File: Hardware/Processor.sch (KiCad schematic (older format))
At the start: 15 parts, among them J1 ICSP-PIC, J2 USB_MINI, SW1 PGM, SW2 RST, U5 PIC32MX250F128B, X1 8MHz

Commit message: Initial component mapping
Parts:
- J2: Distributor Part No (none) -> ED2992CT-ND; MFR Name (none) -> On Shore Technology; MFR Part No (none) -> USB-M26FTR
- X1: Distributor Part No (none) -> 535-9831-1-ND; MFR Name (none) -> Abracon; MFR Part No (none) -> ABM7-8.000MHZ-D2Y-T
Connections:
- wire segments 72 -> 63
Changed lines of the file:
@@
 $EndComp
 $Comp
-L +3.3V #PWR32
+L +3.3V #PWR031
 U 1 1 5240FDA6
 P 2500 1800
-F 0 "#PWR32" H 2500 1760 30  0001 C CNN
+F 0 "#PWR031" H 2500 1760 30  0001 C CNN
 F 1 "+3.3V" H 2500 1910 30  0000 C CNN
 F 2 "" H 2500 1800 60  0000 C CNN
@@
 $EndComp
 $Comp
-L GND #PWR35
+L GND #PWR032
 U 1 1 5240FDF5
 P 2500 3100
-F 0 "#PWR35" H 2500 3100 30  0001 C CNN
+F 0 "#PWR032" H 2500 3100 30  0001 C CNN
 F 1 "GND" H 2500 3030 30  0001 C CNN
 F 2 "" H 2500 3100 60  0000 C CNN
@@
 F 2 "~" H 2450 5200 60  0000 C CNN
 F 3 "~" H 2450 5200 60  0000 C CNN
+F 4 "Abracon" H 2450 5200 60  0001 C CNN "MFR Name"
+F 5 "ABM7-8.000MHZ-D2Y-T" H 2450 5200 60  0001 C CNN "MFR Part No"
+F 6 "535-9831-1-ND" H 2450 5200 60  0001 C CNN "Distributor Part No"
 	1    2450 5200
 	1    0    0    -1
@@
 OSC2
 $Comp
-L GND #PWR41
+L GND #PWR033
 U 1 1 5240FF54
 P 2100 5900
-F 0 "#PWR41" H 2100 5900 30  0001 C CNN
+F 0 "#PWR033" H 2100 5900 30  0001 C CNN
 F 1 "GND" H 2100 5830 30  0001 C CNN
 F 2 "" H 2100 5900 60  0000 C CNN
@@
 $EndComp
 $Comp
-L GND #PWR42
+L GND #PWR034
 U 1 1 5240FF63
 P 2800 5900
-F 0 "#PWR42" H 2800 5900 30  0001 C CNN
+F 0 "#PWR034" H 2800 5900 30  0001 C CNN
 F 1 "GND" H 2800 5830 30  0001 C CNN
 F 2 "" H 2800 5900 60  0000 C CNN
@@
 F 2 "~" H 2000 3850 60  0000 C CNN
 F 3 "~" H 2000 3850 60  0000 C CNN
+F 4 "On Shore Technology" H 2000 3850 60  0001 C CNN "MFR Name"
+F 5 "USB-M26FTR" H 2000 3850 60  0001 C CNN "MFR Part No"
+F 6 "ED2992CT-ND" H 2000 3850 60  0001 C CNN "Distributor Part No"
 	1    2000 3850
 	-1   0    0    -1
@@
 $EndComp
 $Comp
-L +3.3V #PWR37
+L +3.3V #PWR035
 U 1 1 5240FFFE
 P 6800 3300
-F 0 "#PWR37" H 6800 3260 30  0001 C CNN
+F 0 "#PWR035" H 6800 3260 30  0001 C CNN
 F 1 "+3.3V" H 6800 3410 30  0000 C CNN
 F 2 "" H 6800 3300 60  0000 C CNN
@@
 $EndComp
 $Comp
-L GND #PWR40
+L GND #PWR036
 U 1 1 52410043
 P 6900 4900
-F 0 "#PWR40" H 6900 4900 30  0001 C CNN
+F 0 "#PWR036" H 6900 4900 30  0001 C CNN
 F 1 "GND" H 6900 4830 30  0001 C CNN
 F 2 "" H 6900 4900 60  0000 C CNN
@@
 $EndComp
 $Comp
-L +3.3V #PWR36
+L +3.3V #PWR037
 U 1 1 524100A6
 P 5400 3300
-F 0 "#PWR36" H 5400 3260 30  0001 C CNN
+F 0 "#PWR037" H 5400 3260 30  0001 C CNN
 F 1 "+3.3V" H 5400 3410 30  0000 C CNN
 F 2 "" H 5400 3300 60  0000 C CNN
@@
 $EndComp
 $Comp
-L GND #PWR39
+L GND #PWR038
 U 1 1 524100D5
 P 5300 4900
-F 0 "#PWR39" H 5300 4900 30  0001 C CNN
+F 0 "#PWR038" H 5300 4900 30  0001 C CNN
 F 1 "GND" H 5300 4830 30  0001 C CNN
 F 2 "" H 5300 4900 60  0000 C CNN
@@
 $EndComp
 $Comp
-L GND #PWR44
+L GND #PWR039
 U 1 1 5241010B
 P 2100 7200
-F 0 "#PWR44" H 2100 7200 30  0001 C CNN
+F 0 "#PWR039" H 2100 7200 30  0001 C CNN
 F 1 "GND" H 2100 7130 30  0001 C CNN
 F 2 "" H 2100 7200 60  0000 C CNN
@@
 $EndComp
 Wire Wire Line
-	2500 1800 2500 1900
-Wire Wire Line
-	2500 1900 2500 2700
+	2500 1800 2500 2700
 Wire Wire Line
 	2500 2700 2400 2700
@@
 	2500 2800 2500 3100
 Wire Wire Line
-	2400 2600 2700 2600
-Wire Wire Line
-	2700 2600 2800 2600
+	2400 2600 2800 2600
 Wire Wire Line
 	2700 2500 2700 2600
@@
 	2400 3000 2800 3000
 Wire Wire Line
-	2800 5100 2800 5200
-Wire Wire Line
-	2800 5200 2800 5300
-Wire Wire Line
-	2100 5100 2100 5200
-Wire Wire Line
-	2100 5200 2100 5300
+	2800 5100 2800 5300
+Wire Wire Line
+	2100 5100 2100 5300
 Wire Wire Line
 	2200 5200 2100 5200
@@
 	7000 3600 6700 3600
 Wire Wire Line
-	6800 3300 6800 3700
-Wire Wire Line
-	6800 3700 6800 4300
+	6800 3300 6800 4300
 Wire Wire Line
 	6800 3700 6700 3700
 Wire Wire Line
-	6900 3800 6900 4700
-Wire Wire Line
-	6900 4700 6900 4900
+	6900 3800 6900 4900
 Wire Wire Line
 	6900 3800 6700 3800
@@
 	2100 6500 2100 6600
 $Comp
-L GND #PWR38
+L GND #PWR040
 U 1 1 524101F5
 P 2400 4200
-F 0 "#PWR38" H 2400 4200 30  0001 C CNN
+F 0 "#PWR040" H 2400 4200 30  0001 C CNN
 F 1 "GND" H 2400 4130 30  0001 C CNN
 F 2 "" H 2400 4200 60  0000 C CNN
@@
 	2400 4100 2400 4200
 $Comp
-L +3.3V #PWR43
+L +3.3V #PWR041
 U 1 1 524102C8
 P 3000 6400
-F 0 "#PWR43" H 3000 6360 30  0001 C CNN
+F 0 "#PWR041" H 3000 6360 30  0001 C CNN
 F 1 "+3.3V" H 3000 6510 30  0000 C CNN
 F 2 "" H 3000 6400 60  0000 C CNN
@@
 	2700 6600 2700 6500
 Wire Wire Line
-	2700 6500 3000 6500
-Wire Wire Line
-	3000 6500 3300 6500
+	2700 6500 3300 6500
 Wire Wire Line
 	2700 7100 2700 7200
 Wire Wire Line
-	2700 7200 3000 7200
-Wire Wire Line
-	3000 7200 3300 7200
-$Comp
-L GND #PWR45
+	2700 7200 3300 7200
+$Comp
+L GND #PWR042
 U 1 1 5241033E
 P 3000 7300
-F 0 "#PWR45" H 3000 7300 30  0001 C CNN
+F 0 "#PWR042" H 3000 7300 30  0001 C CNN
 F 1 "GND" H 3000 7230 30  0001 C CNN
 F 2 "" H 3000 7300 60  0000 C CNN
@@
 	4700 1300 4800 1300
 Wire Wire Line
-	5300 1300 5400 1300
-Wire Wire Line
-	5400 1300 5500 1300
-$Comp
-L GND #PWR33
+	5300 1300 5500 1300
+$Comp
+L GND #PWR043
 U 1 1 5241051A
 P 5400 2000
-F 0 "#PWR33" H 5400 2000 30  0001 C CNN
+F 0 "#PWR043" H 5400 2000 30  0001 C CNN
 F 1 "GND" H 5400 1930 30  0001 C CNN
 F 2 "" H 5400 2000 60  0000 C CNN
@@
 $EndComp
 $Comp
-L +3.3V #PWR31
+L +3.3V #PWR044
 U 1 1 52410529
 P 6100 1200
-F 0 "#PWR31" H 6100 1160 30  0001 C CNN
+F 0 "#PWR044" H 6100 1160 30  0001 C CNN
 F 1 "+3.3V" H 6100 1310 30  0000 C CNN
 F 2 "" H 6100 1200 60  0000 C CNN
@@
 $EndComp
 $Comp
-L GND #PWR34
+L GND #PWR045
 U 1 1 52410620
 P 6100 2400
-F 0 "#PWR34" H 6100 2400 30  0001 C CNN
+F 0 "#PWR045" H 6100 2400 30  0001 C CNN
 F 1 "GND" H 6100 2330 30  0001 C CNN
 F 2 "" H 6100 2400 60  0000 C CNN

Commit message: Associate switches
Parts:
- SW1, SW2: Distributor Part No (none) -> EG4621CT-ND; MFR Name (none) -> E-Switch; MFR Part No (none) -> TL3315NF160Q
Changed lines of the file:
@@
 Sheet 5 8
 Title "Solid State Cosmic Ray Detector"
-Date "24 sep 2013"
+Date "26 sep 2013"
 Rev "1"
 Comp "Ethan Harstad"
@@
 $EndComp
 $Comp
-L +3.3V #PWR32
+L +3.3V #PWR031
 U 1 1 5240FDA6
 P 2500 1800
-F 0 "#PWR32" H 2500 1760 30  0001 C CNN
+F 0 "#PWR031" H 2500 1760 30  0001 C CNN
 F 1 "+3.3V" H 2500 1910 30  0000 C CNN
 F 2 "" H 2500 1800 60  0000 C CNN
@@
 $EndComp
 $Comp
-L GND #PWR35
+L GND #PWR032
 U 1 1 5240FDF5
 P 2500 3100
-F 0 "#PWR35" H 2500 3100 30  0001 C CNN
+F 0 "#PWR032" H 2500 3100 30  0001 C CNN
 F 1 "GND" H 2500 3030 30  0001 C CNN
 F 2 "" H 2500 3100 60  0000 C CNN
@@
 OSC2
 $Comp
-L GND #PWR41
+L GND #PWR033
 U 1 1 5240FF54
 P 2100 5900
-F 0 "#PWR41" H 2100 5900 30  0001 C CNN
+F 0 "#PWR033" H 2100 5900 30  0001 C CNN
 F 1 "GND" H 2100 5830 30  0001 C CNN
 F 2 "" H 2100 5900 60  0000 C CNN
@@
 $EndComp
 $Comp
-L GND #PWR42
+L GND #PWR034
 U 1 1 5240FF63
 P 2800 5900
-F 0 "#PWR42" H 2800 5900 30  0001 C CNN
+F 0 "#PWR034" H 2800 5900 30  0001 C CNN
 F 1 "GND" H 2800 5830 30  0001 C CNN
 F 2 "" H 2800 5900 60  0000 C CNN
@@
 $EndComp
 $Comp
-L +3.3V #PWR37
+L +3.3V #PWR035
 U 1 1 5240FFFE
 P 6800 3300
-F 0 "#PWR37" H 6800 3260 30  0001 C CNN
+F 0 "#PWR035" H 6800 3260 30  0001 C CNN
 F 1 "+3.3V" H 6800 3410 30  0000 C CNN
 F 2 "" H 6800 3300 60  0000 C CNN
@@
 $EndComp
 $Comp
-L GND #PWR40
+L GND #PWR036
 U 1 1 52410043
 P 6900 4900
-F 0 "#PWR40" H 6900 4900 30  0001 C CNN
+F 0 "#PWR036" H 6900 4900 30  0001 C CNN
 F 1 "GND" H 6900 4830 30  0001 C CNN
 F 2 "" H 6900 4900 60  0000 C CNN
@@
 $EndComp
 $Comp
-L +3.3V #PWR36
+L +3.3V #PWR037
 U 1 1 524100A6
 P 5400 3300
-F 0 "#PWR36" H 5400 3260 30  0001 C CNN
+F 0 "#PWR037" H 5400 3260 30  0001 C CNN
 F 1 "+3.3V" H 5400 3410 30  0000 C CNN
 F 2 "" H 5400 3300 60  0000 C CNN
@@
 $EndComp
 $Comp
-L GND #PWR39
+L GND #PWR038
 U 1 1 524100D5
 P 5300 4900
-F 0 "#PWR39" H 5300 4900 30  0001 C CNN
+F 0 "#PWR038" H 5300 4900 30  0001 C CNN
 F 1 "GND" H 5300 4830 30  0001 C CNN
 F 2 "" H 5300 4900 60  0000 C CNN
@@
 $EndComp
 $Comp
-L GND #PWR44
+L GND #PWR039
 U 1 1 5241010B
 P 2100 7200
-F 0 "#PWR44" H 2100 7200 30  0001 C CNN
+F 0 "#PWR039" H 2100 7200 30  0001 C CNN
 F 1 "GND" H 2100 7130 30  0001 C CNN
 F 2 "" H 2100 7200 60  0000 C CNN
@@
 	2100 6500 2100 6600
 $Comp
-L GND #PWR38
+L GND #PWR040
 U 1 1 524101F5
 P 2400 4200
-F 0 "#PWR38" H 2400 4200 30  0001 C CNN
+F 0 "#PWR040" H 2400 4200 30  0001 C CNN
 F 1 "GND" H 2400 4130 30  0001 C CNN
 F 2 "" H 2400 4200 60  0000 C CNN
@@
 	2400 4100 2400 4200
 $Comp
-L +3.3V #PWR43
+L +3.3V #PWR041
 U 1 1 524102C8
 P 3000 6400
-F 0 "#PWR43" H 3000 6360 30  0001 C CNN
+F 0 "#PWR041" H 3000 6360 30  0001 C CNN
 F 1 "+3.3V" H 3000 6510 30  0000 C CNN
 F 2 "" H 3000 6400 60  0000 C CNN
@@
 	2700 7200 3300 7200
 $Comp
-L GND #PWR45
+L GND #PWR042
 U 1 1 5241033E
 P 3000 7300
-F 0 "#PWR45" H 3000 7300 30  0001 C CNN
+F 0 "#PWR042" H 3000 7300 30  0001 C CNN
 F 1 "GND" H 3000 7230 30  0001 C CNN
 F 2 "" H 3000 7300 60  0000 C CNN
@@
 F 2 "~" H 5750 1300 60  0000 C CNN
 F 3 "~" H 5750 1300 60  0000 C CNN
+F 4 "E-Switch" H 5750 1300 60  0001 C CNN "MFR Name"
+F 5 "TL3315NF160Q" H 5750 1300 60  0001 C CNN "MFR Part No"
+F 6 "EG4621CT-ND" H 5750 1300 60  0001 C CNN "Distributor Part No"
 	1    5750 1300
 	1    0    0    -1
@@
 	5300 1300 5500 1300
 $Comp
-L GND #PWR33
+L GND #PWR043
 U 1 1 5241051A
 P 5400 2000
-F 0 "#PWR33" H 5400 2000 30  0001 C CNN
+F 0 "#PWR043" H 5400 2000 30  0001 C CNN
 F 1 "GND" H 5400 1930 30  0001 C CNN
 F 2 "" H 5400 2000 60  0000 C CNN
@@
 $EndComp
 $Comp
-L +3.3V #PWR31
+L +3.3V #PWR044
 U 1 1 52410529
 P 6100 1200
-F 0 "#PWR31" H 6100 1160 30  0001 C CNN
+F 0 "#PWR044" H 6100 1160 30  0001 C CNN
 F 1 "+3.3V" H 6100 1310 30  0000 C CNN
 F 2 "" H 6100 1200 60  0000 C CNN
@@
 	5400 1900 5400 2000
 $Comp
-L SW-MOM SW2
-U 1 1 52410607
-P 5750 2300
-F 0 "SW2" H 5750 2450 60  0000 C CNN
-F 1 "RST" H 5750 2200 60  0000 C CNN
-F 2 "~" H 5750 2300 60  0000 C CNN
-F 3 "~" H 5750 2300 60  0000 C CNN
-	1    5750 2300
-	1    0    0    -1
-$EndComp
-$Comp
-L GND #PWR34
+L GND #PWR045
 U 1 1 52410620
 P 6100 2400
-F 0 "#PWR34" H 6100 2400 30  0001 C CNN
+F 0 "#PWR045" H 6100 2400 30  0001 C CNN
 F 1 "GND" H 6100 2330 30  0001 C CNN
 F 2 "" H 6100 2400 60  0000 C CNN
@@
 	0    1    1    0
 $EndComp
+$Comp
+L SW-MOM SW2
+U 1 1 5243E5AD
+P 5750 2300
+F 0 "SW2" H 5750 2450 60  0000 C CNN
+F 1 "RST" H 5750 2200 60  0000 C CNN
+F 2 "~" H 5750 2300 60  0000 C CNN
+F 3 "~" H 5750 2300 60  0000 C CNN
+F 4 "E-Switch" H 5750 2300 60  0001 C CNN "MFR Name"
+F 5 "TL3315NF160Q" H 5750 2300 60  0001 C CNN "MFR Part No"
+F 6 "EG4621CT-ND" H 5750 2300 60  0001 C CNN "Distributor Part No"
+	1    5750 2300
+	1    0    0    -1
+$EndComp
 $EndSCHEMATC

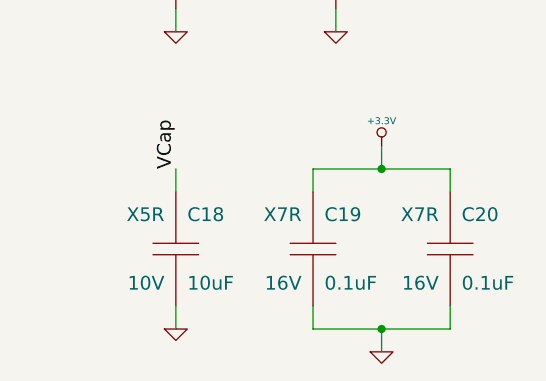
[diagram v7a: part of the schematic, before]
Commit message: Add 12v regulator and populate BOM fields
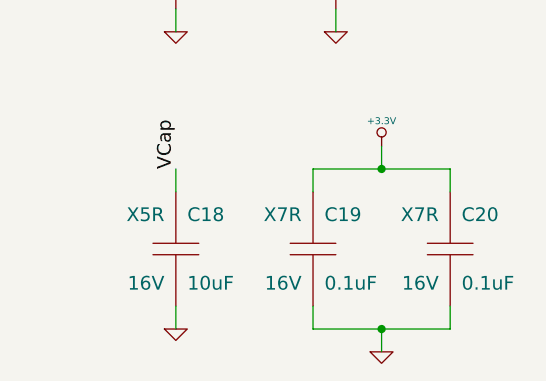
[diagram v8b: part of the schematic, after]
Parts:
- C18: Distributor Part No 1276-1052-1-ND -> 587-1295-1-ND; MFR Name Samsung -> Taiyo Yuden; MFR Part No CL21A106KPFNNNE -> EMK212BJ106KG-T; Voltage 10V -> 16V
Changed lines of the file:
@@
 Sheet 5 8
 Title "Solid State Cosmic Ray Detector"
-Date "26 sep 2013"
+Date "27 sep 2013"
 Rev "1"
 Comp "Ethan Harstad"
@@
 F 2 "CAPC2012" H 2100 6850 60  0001 C CNN
 F 3 "~" H 2100 6850 60  0000 C CNN
-F 4 "Samsung" H 2100 6850 60  0001 C CNN "MFR Name"
-F 5 "CL21A106KPFNNNE" H 2100 6850 60  0001 C CNN "MFR Part No"
-F 6 "1276-1052-1-ND" H 2100 6850 60  0001 C CNN "Distributor Part No"
-F 7 "10V" H 2050 6700 60  0000 R CNN "Voltage"
+F 4 "Taiyo Yuden" H 2100 6850 60  0001 C CNN "MFR Name"
+F 5 "EMK212BJ106KG-T" H 2100 6850 60  0001 C CNN "MFR Part No"
+F 6 "587-1295-1-ND" H 2100 6850 60  0001 C CNN "Distributor Part No"
+F 7 "16V" H 2050 6700 60  0000 R CNN "Voltage"
 F 8 "X5R" H 2050 7000 60  0000 R CNN "Dielectric"
 	1    2100 6850
